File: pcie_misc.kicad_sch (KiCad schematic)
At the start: 33 parts, among them U30 9DBL0651CKILF, U31 74AUP2G132, Y1 Oscillator_32.768kHz_ECS_2520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

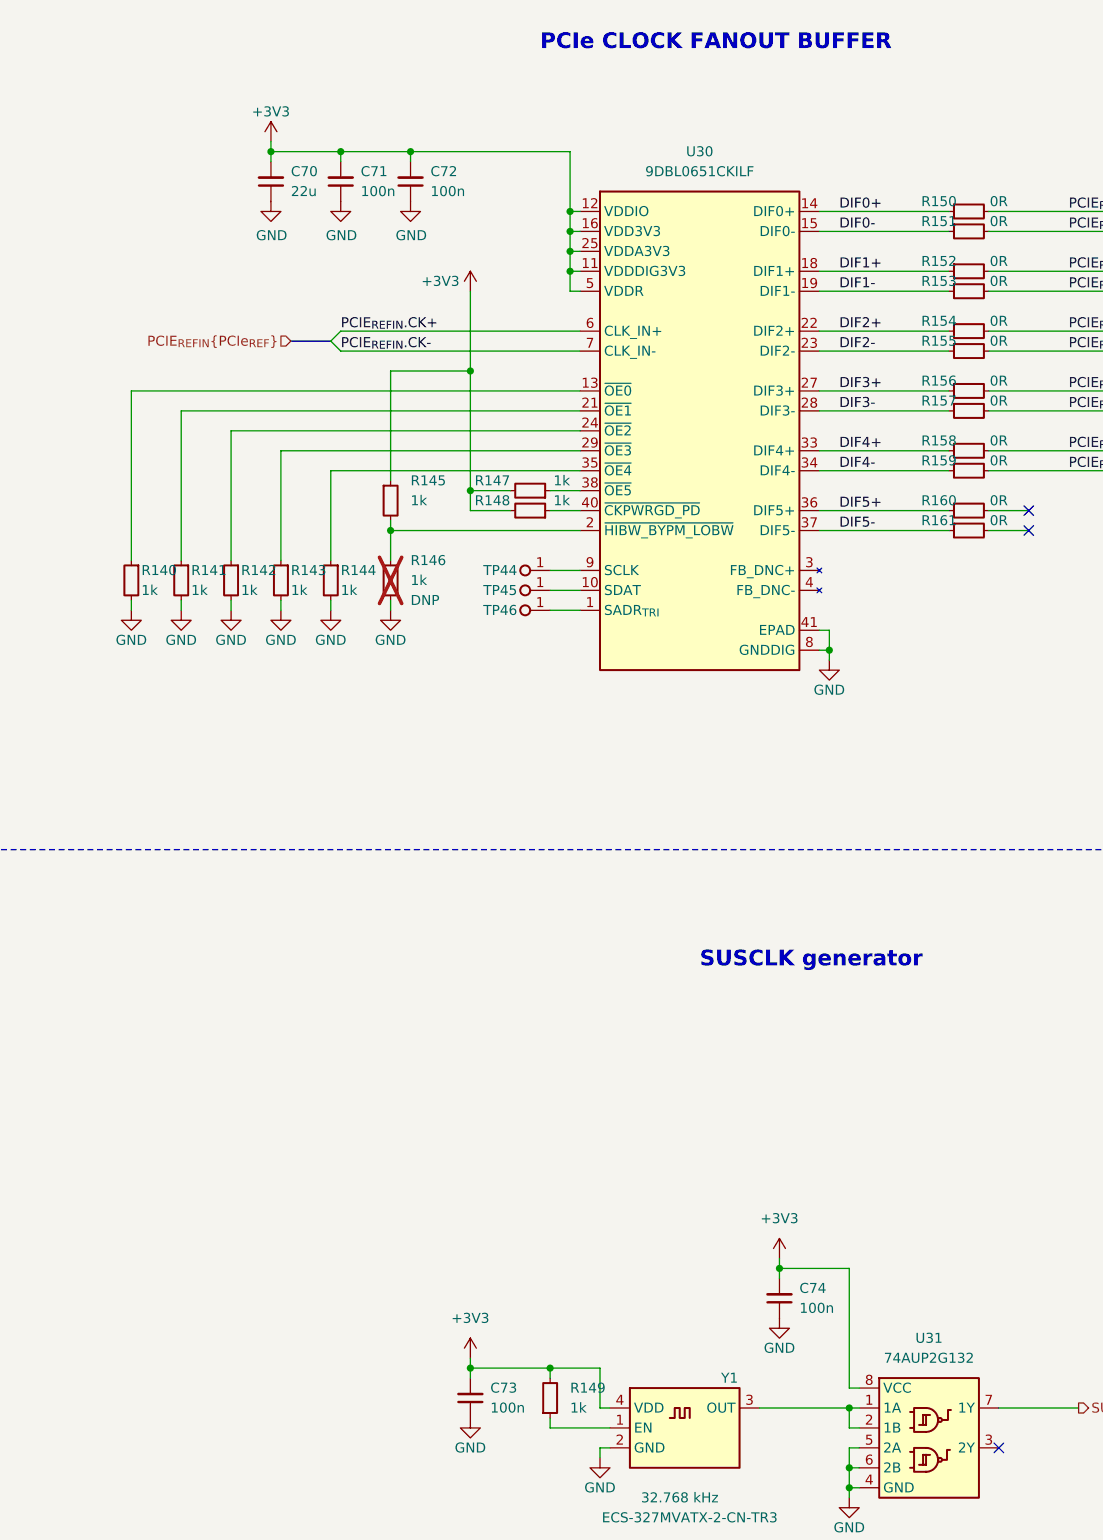
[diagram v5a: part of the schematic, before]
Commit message: Reannotate schematic
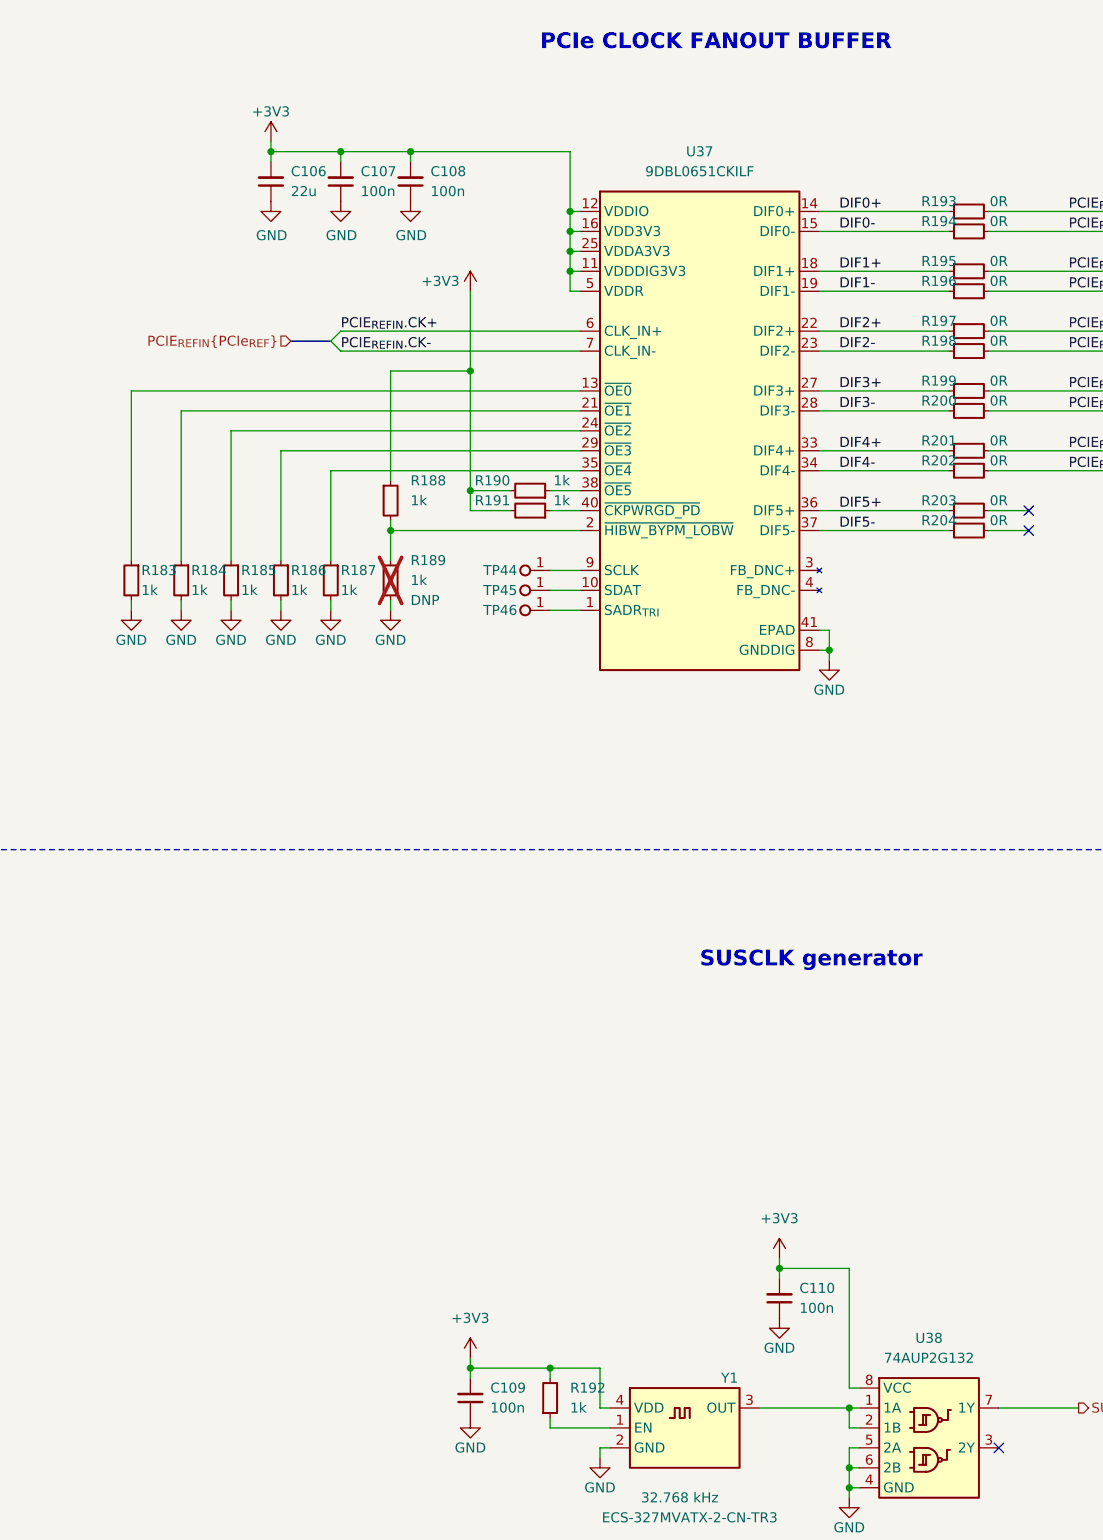
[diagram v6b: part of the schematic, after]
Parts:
- renumbered C70 to C106, C71 to C107, C72 to C108, C73 to C109, C74 to C110, R140 to R183, R141 to R184, R142 to R185, R143 to R186, R144 to R187, R145 to R188, R146 to R189, R147 to R190, R148 to R191, R149 to R192, R150 to R193, R151 to R194, R152 to R195, R153 to R196, R154 to R197, R155 to R198, R156 to R199, R157 to R200, R158 to R201, R159 to R202, R160 to R203, R161 to R204, U30 to U37, U31 to U38

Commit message: Optimize BOM, reannotate
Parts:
- removed R203, R204: R_0R_0402, antmicro-footprints:R_0402_1005Metric, symbol antmicroResistors0402:R_0R_0402
- added TP47, TP48: TP_0.75mm_SMD, antmicro-footprints:TP_SMD_0.75mm, symbol antmicroTestPoints:TP_0.75mm_SMD
- renumbered R183 to R182, R184 to R183, R185 to R184, R186 to R185, R187 to R186, R188 to R187, R189 to R188, R190 to R189, R191 to R190, R192 to R191, R193 to R192, R194 to R193, R195 to R194, R196 to R195, R197 to R196, R198 to R197, R199 to R198, R200 to R199, R201 to R200, R202 to R201
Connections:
- net DIF5+: now also TP47.1
- net DIF5-: now also TP48.1
- no-connect marks 3 -> 1

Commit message: [#58137] Update 9DBL0651CKILF from lib
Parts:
- U37: footprint antmicro-footprints:UQFN-40-1EP_5x5mm_P0.4mm_EP3.8x3.8mm -> antmicro-footprints:VFQFPN-40-1EP_5x5mm_P0.4mm_EP3.5x3.5mm
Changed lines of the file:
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@@
       (effects (font (size 1.27 1.27) (thickness 0.15)) (justify left bottom) hide)
     )
-    (property "Footprint" "antmicro-footprints:UQFN-40-1EP_5x5mm_P0.4mm_EP3.8x3.8mm" (at 134.62 66.04 0)
+    (property "Footprint" "antmicro-footprints:VFQFPN-40-1EP_5x5mm_P0.4mm_EP3.5x3.5mm" (at 134.62 66.04 0)
       (effects (font (size 1.27 1.27) (thickness 0.15)) (justify left bottom) hide)
     )
